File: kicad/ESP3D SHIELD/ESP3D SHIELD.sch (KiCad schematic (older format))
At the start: 12 parts, among them Q1 BSS138, Q2 BSS138, SW1 RESET, SW2 PROGRAM, SW3 RESET_CONFIG, U1 LM1117-3.3, U2 ESP-12E

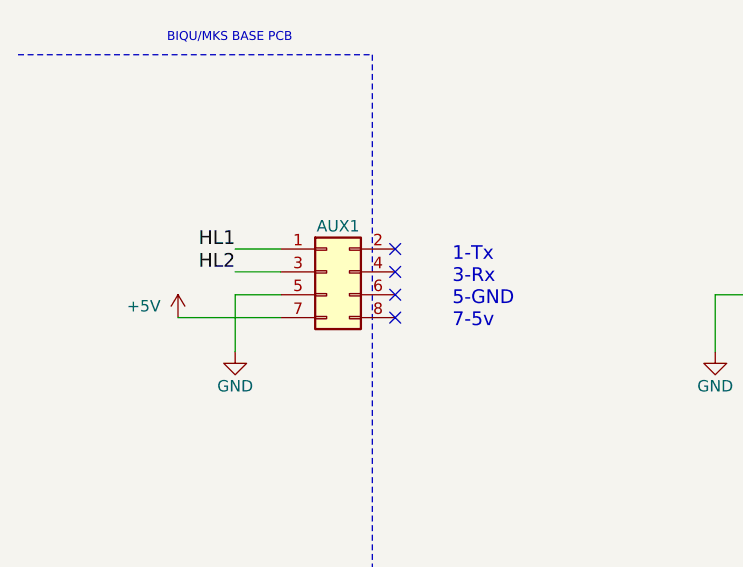
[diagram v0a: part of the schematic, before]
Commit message: connector is now IDC , bigger board
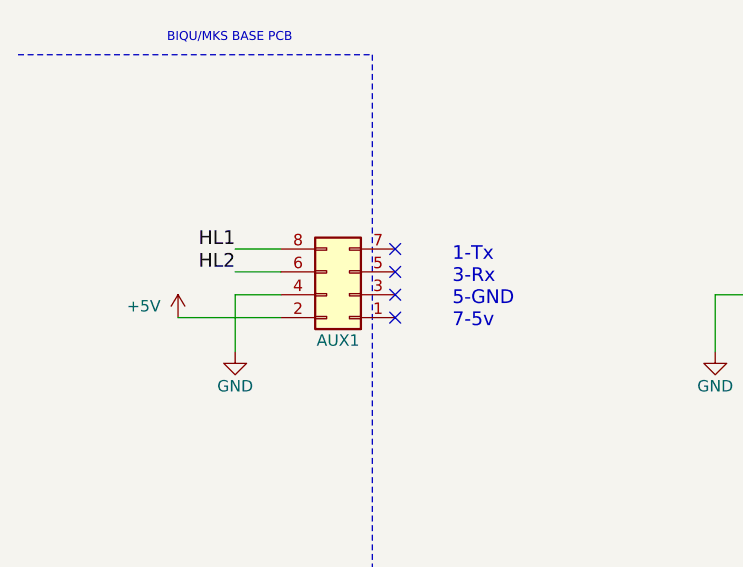
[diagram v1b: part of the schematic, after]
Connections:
- net +5V: now also AUX1.2 (Pin_2); no longer AUX1.7 (Pin_7)
- net GND: now also AUX1.4 (Pin_4); no longer AUX1.5 (Pin_5)
- net HL1: now also AUX1.8 (Pin_8); no longer AUX1.1 (Pin_1)
- net HL2: now also AUX1.6 (Pin_6); no longer AUX1.3 (Pin_3)
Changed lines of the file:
@@
 L Conn_02x04_Odd_Even AUX1
 U 1 1 59CE59F3
-P 2150 2550
-F 0 "AUX1" H 2200 2750 50  0000 C CNN
-F 1 "Conn_02x04_Odd_Even" H 2350 2950 50  0001 C CNN
-F 2 "Socket_Strips:Socket_Strip_Straight_2x04_Pitch2.54mm" H 2150 2550 50  0001 C CNN
-F 3 "" H 2150 2550 50  0001 C CNN
-	1    2150 2550
-	1    0    0    -1
+P 2250 2650
+F 0 "AUX1" H 2300 2850 50  0000 C CNN
+F 1 "Conn_02x04_Odd_Even" H 2450 3050 50  0001 C CNN
+F 2 "Socket_Strips:Socket_Strip_Straight_2x04_Pitch2.54mm" H 2250 2650 50  0001 C CNN
+F 3 "" H 2250 2650 50  0001 C CNN
+	1    2250 2650
+	-1   0    0    1
 $EndComp
 $Comp

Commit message: revB final
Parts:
- AUX1: footprint Socket_Strips:Socket_Strip_Straight_2x04_Pitch2.54mm -> Connectors:IDC_Header_Straight_8pins
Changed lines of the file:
@@
 F 0 "AUX1" H 2300 2850 50  0000 C CNN
 F 1 "Conn_02x04_Odd_Even" H 2450 3050 50  0001 C CNN
-F 2 "Socket_Strips:Socket_Strip_Straight_2x04_Pitch2.54mm" H 2250 2650 50  0001 C CNN
+F 2 "Connectors:IDC_Header_Straight_8pins" H 2250 2650 50  0001 C CNN
 F 3 "" H 2250 2650 50  0001 C CNN
 	1    2250 2650
